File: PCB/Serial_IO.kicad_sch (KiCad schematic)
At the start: 35 parts, among them Q1 BC213C, Q2 BC213C, Q3 BC184C, Q6 BC184C, U8 MAX232

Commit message: feat: Upload initial PCB v0.3
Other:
- title: ZXTeensyIF1 -> ${PRJ_NAME}
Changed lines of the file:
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@@
 	(paper "A4")
 	(title_block
-		(title "ZXTeensyIF1")
-		(date "2026-01-04")
-		(rev "0.1")
+		(title "${PRJ_NAME}")
+		(date "${PRJ_DATE}")
+		(rev "${PRJ_REVISION}")
 	)
 	(junction

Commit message: feat: Add ESP-01S header to PCB v0.5
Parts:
- D7: footprint Diode_THT:D_DO-35_SOD27_P10.16mm_Horizontal -> Diode_THT:D_DO-35_SOD27_P7.62mm_Horizontal
- R6: footprint Resistor_THT:R_Axial_DIN0207_L6.3mm_D2.5mm_P10.16mm_Horizontal -> Resistor_THT:R_Axial_DIN0207_L6.3mm_D2.5mm_P7.62mm_Horizontal
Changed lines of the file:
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@@
 			)
 		)
-		(property "Footprint" "Resistor_THT:R_Axial_DIN0207_L6.3mm_D2.5mm_P10.16mm_Horizontal"
+		(property "Footprint" "Resistor_THT:R_Axial_DIN0207_L6.3mm_D2.5mm_P7.62mm_Horizontal"
 			(at 68.072 45.72 90)
 			(effects
@@
 			)
 		)
-		(property "Footprint" "Diode_THT:D_DO-35_SOD27_P10.16mm_Horizontal"
+		(property "Footprint" "Diode_THT:D_DO-35_SOD27_P7.62mm_Horizontal"
 			(at 41.91 166.37 0)
 			(effects

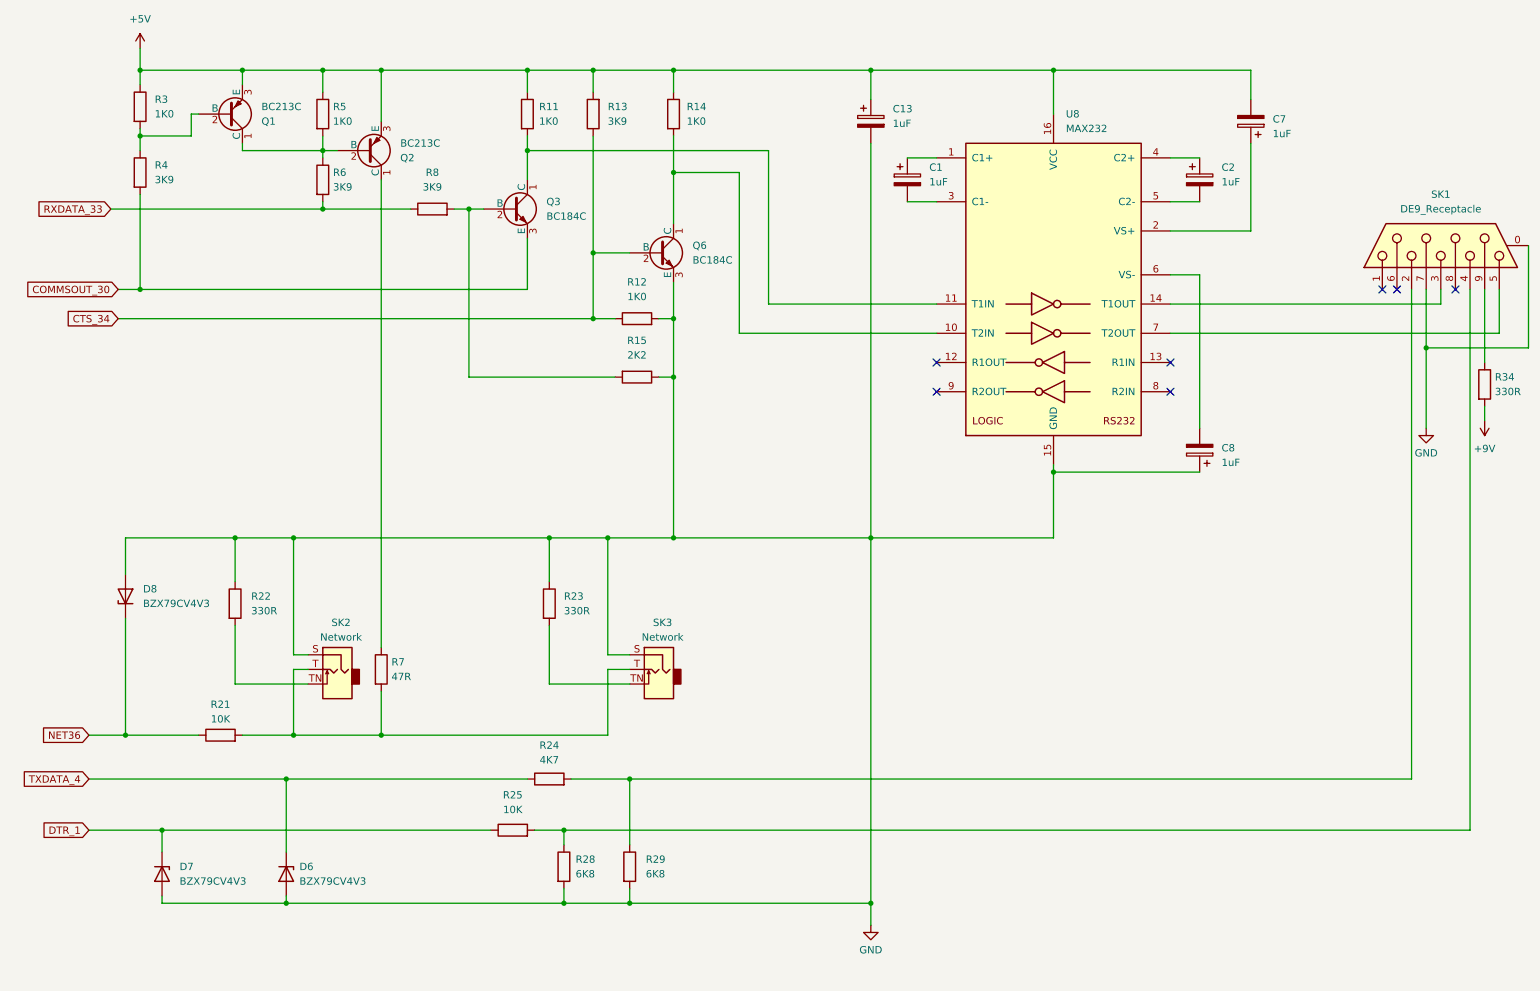
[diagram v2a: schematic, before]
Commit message: Use active DTR and TXDATA from MAX232
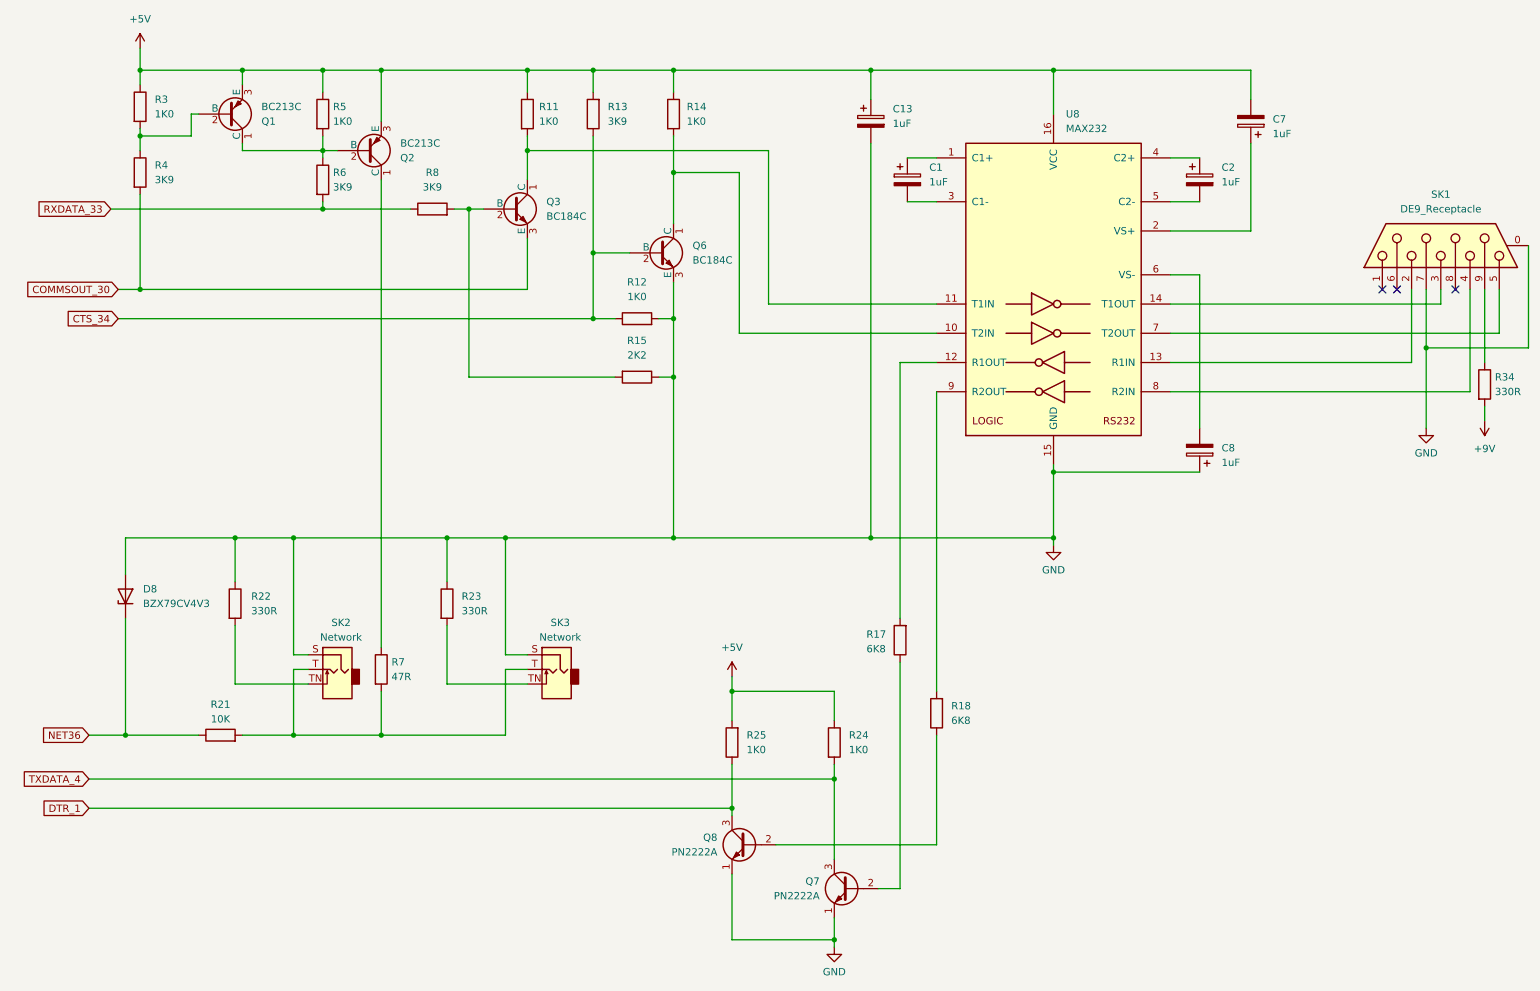
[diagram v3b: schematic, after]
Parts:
- removed D6: BZX79CV4V3, Diode_THT:D_DO-35_SOD27_P10.16mm_Horizontal, symbol Device:D_Zener
- removed D7: BZX79CV4V3, Diode_THT:D_DO-35_SOD27_P7.62mm_Horizontal, symbol Device:D_Zener
- removed R28, R29: 6K8, Resistor_THT:R_Axial_DIN0207_L6.3mm_D2.5mm_P10.16mm_Horizontal, symbol Device:R
- added Q7, Q8: PN2222A, Package_TO_SOT_THT:TO-92_Inline_Wide, symbol Transistor_BJT:PN2222A
- added R17, R18: 6K8, Resistor_THT:R_Axial_DIN0207_L6.3mm_D2.5mm_P10.16mm_Horizontal, symbol Device:R
- R24: value 4K7 -> 1K0
- R25: value 10K -> 1K0
- R6: footprint Resistor_THT:R_Axial_DIN0207_L6.3mm_D2.5mm_P7.62mm_Horizontal -> Resistor_THT:R_Axial_DIN0207_L6.3mm_D2.5mm_P10.16mm_Horizontal
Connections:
- net +5V: now also R24.1, R25.2
- net DTR_1: now also Q8.3 (C)
- net GND: now also Q7.1 (E), Q8.1 (E)
- net TXDATA_4: now also R24.2, Q7.3 (C); no longer R24.1
- net at SK1.4: now also U8.8 (R2IN); no longer R25.2
- net at SK1.2: now also U8.13 (R1IN); no longer R24.2
- net at U8.12 (R1OUT): now also R17.2
- net at U8.9 (R2OUT): now also R18.2
- new net: Q8.2 (B), R18.1
- new net: Q7.2 (B), R17.1
- no-connect marks 7 -> 3
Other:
- moved on the sheet: R23, R24, R25, SK3

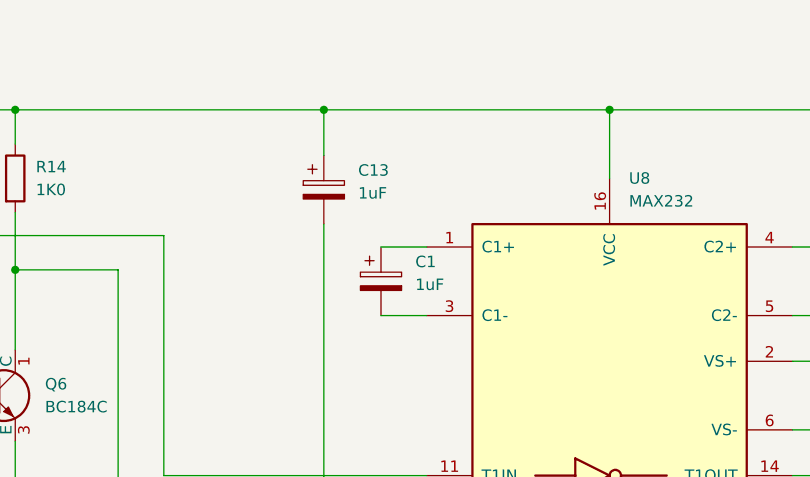
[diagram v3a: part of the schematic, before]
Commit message: PCB move C6 slightly, C13 to 47uF
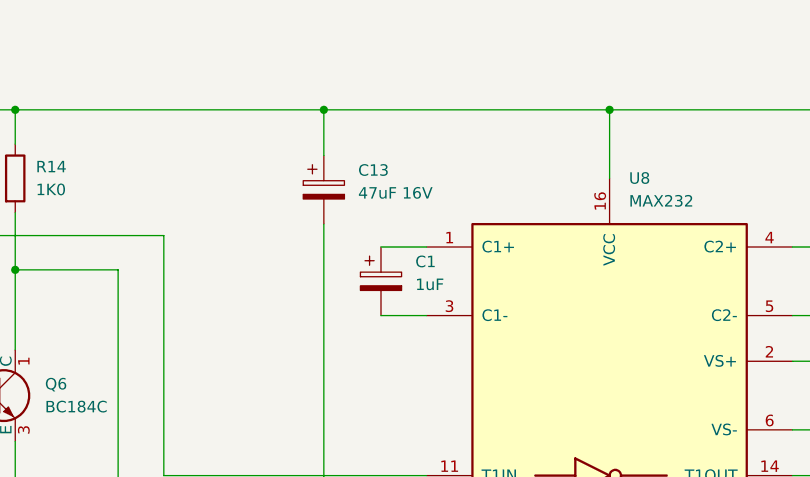
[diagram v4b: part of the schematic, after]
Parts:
- C13: value 1uF -> 47uF 16V
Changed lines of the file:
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@@
 			)
 		)
-		(property "Datasheet" " ~"
+		(property "Datasheet" "~"
 			(at 264.16 57.15 0)
 			(effects
@@
 			)
 		)
-		(property "Value" "1uF"
+		(property "Value" "47uF 16V"
 			(at 168.91 35.9409 0)
 			(effects
